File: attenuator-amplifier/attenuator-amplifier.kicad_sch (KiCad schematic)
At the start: 61 parts, among them J1 IN, J2 AOUT, J3 V_{REF}, J4 COM, J5 PWR, K1 G6KU-2, K2 G6KU-2, K3 G6KU-2, U1 DG4052E, U2 OPA197xDBV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

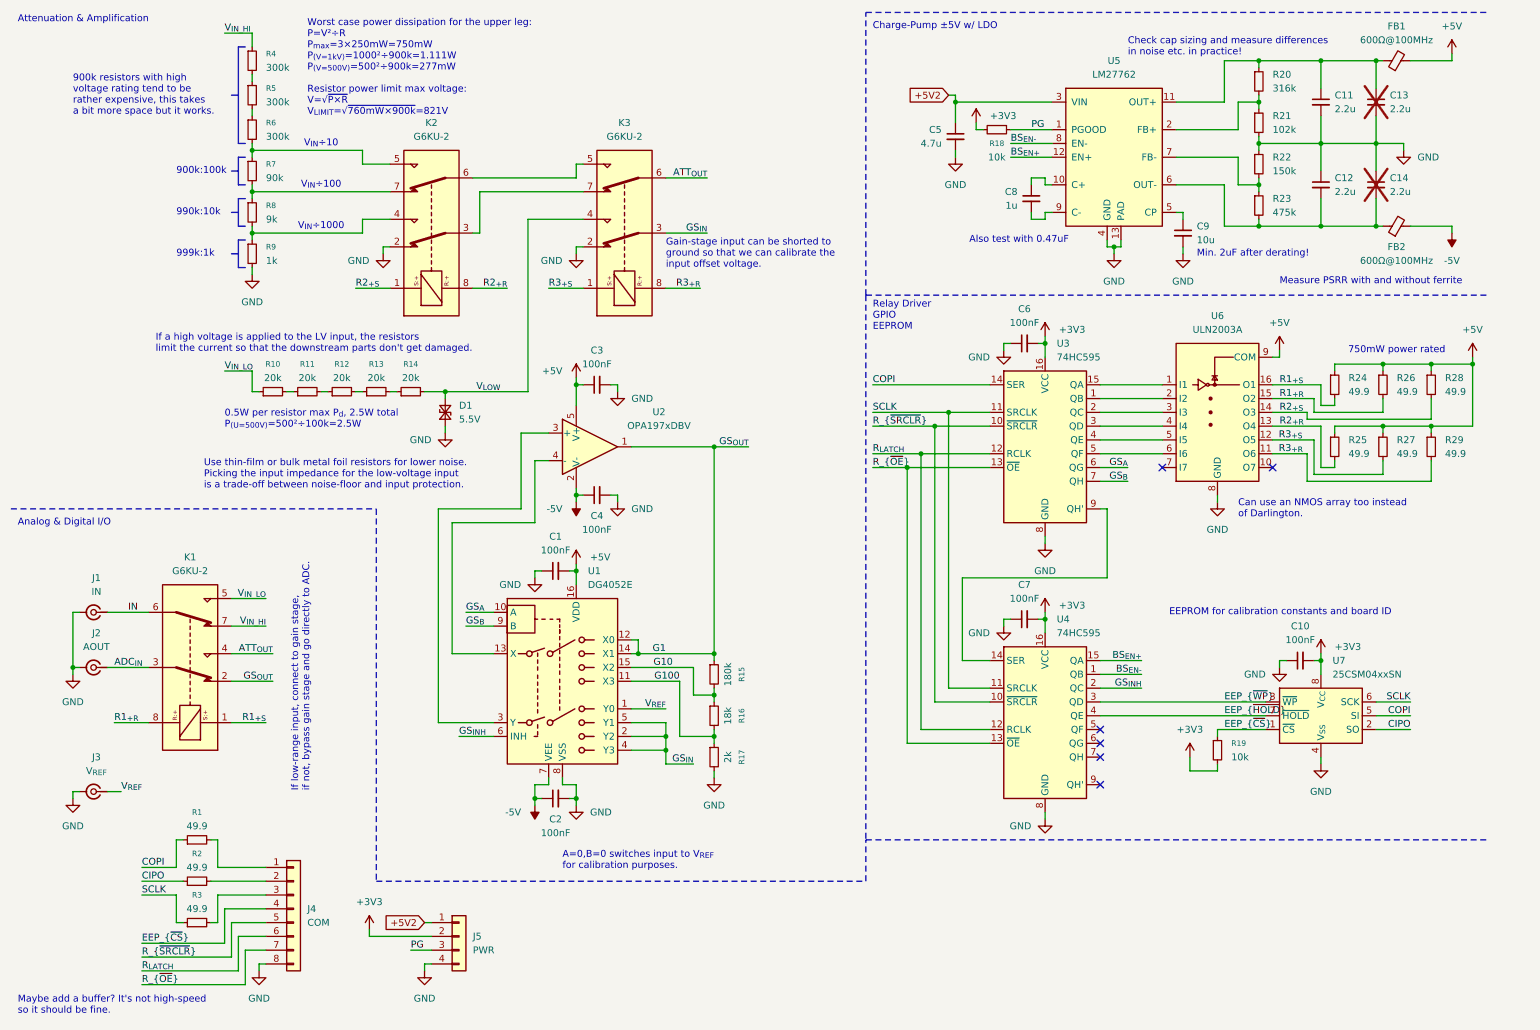
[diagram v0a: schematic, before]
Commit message: small changes, add missing part numbers
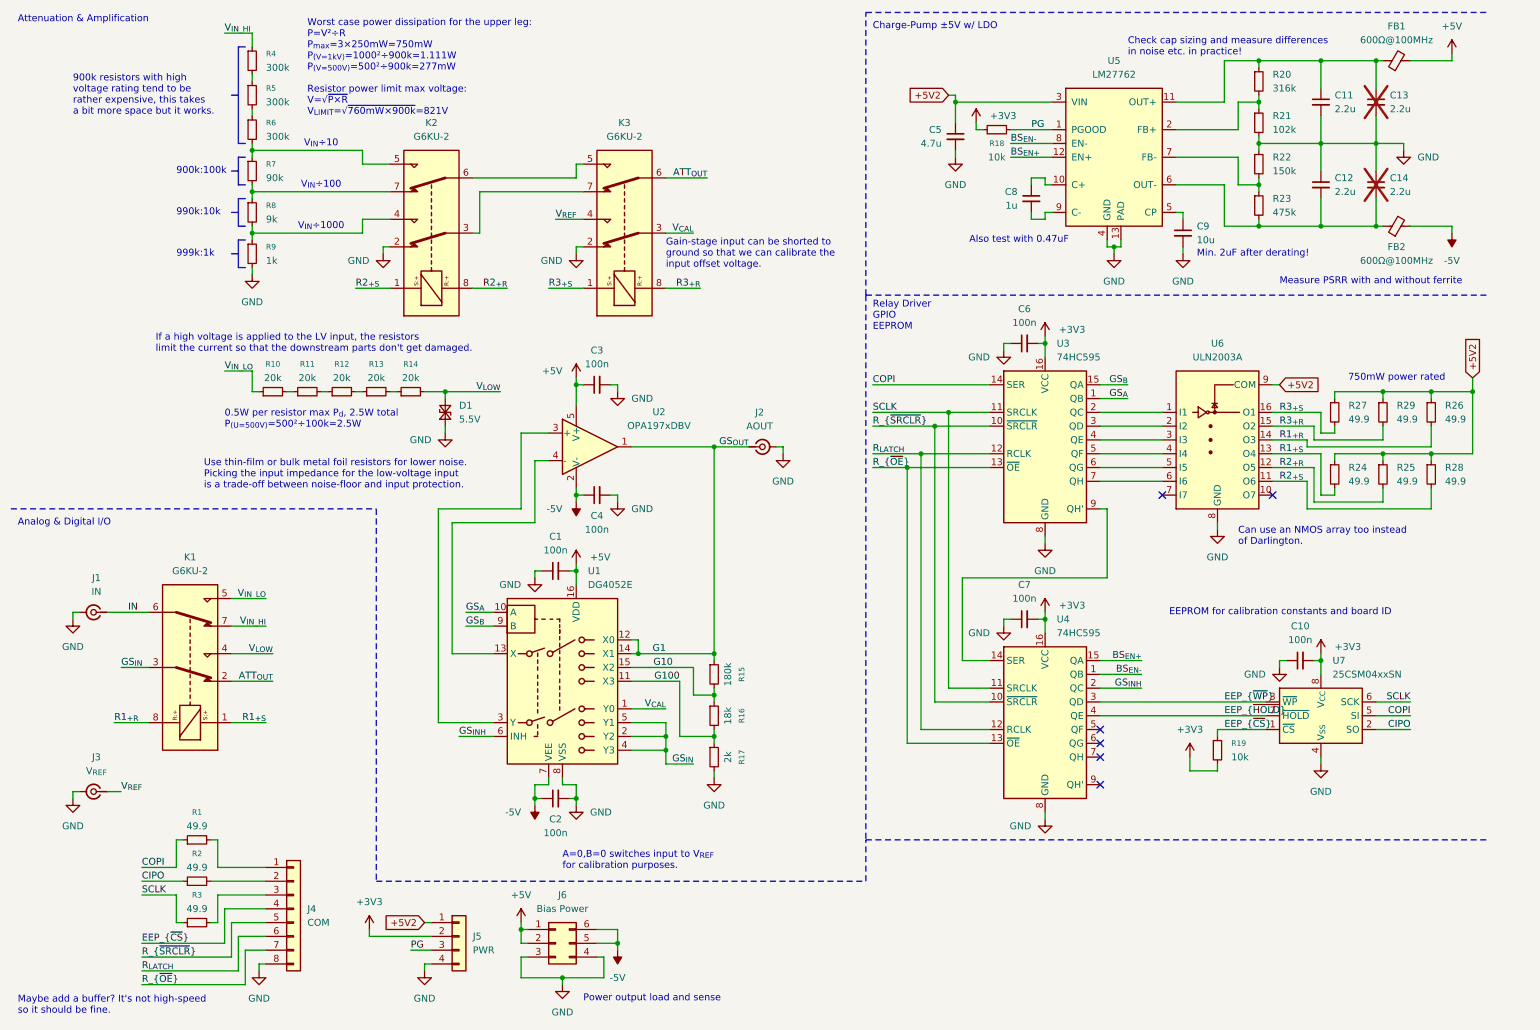
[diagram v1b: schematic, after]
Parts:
- added J6: Bias Power, Connector_PinHeader_2.54mm:PinHeader_2x03_P2.54mm_Vertical, symbol Connector_Generic:Conn_02x03_Counter_Clockwise
- C1, C10, C2, C3, C4, C6, C7: value 100nF -> 100n; MPN (none) -> FN15X104K500PKG
- C11, C12, C13, C14: MPN (none) -> GRM188Z71E225KE43D
- C5: MPN (none) -> TCC0603X7R475K100CT
- C8: MPN (none) -> CGA0603X7R105K250JT
- C9: MPN (none) -> GRM188Z71A106MA73D
- FB1, FB2: MPN (none) -> 74404024220
- J1, J2, J3: MPN (none) -> 61611002121501
- R1, R2, R3: MPN (none) -> 0603WAF499JT5E
- R15: MPN (none) -> RT0603BRB07180KL
- R16: MPN (none) -> RT0603BRB0718KL
- R17: MPN (none) -> AR03BTBX2001
- R18, R19: MPN (none) -> ARG03DTC1002
- R20: MPN (none) -> FRC0402F3163TS
- R21: MPN (none) -> 0402WGF1023TCE
- R22: MPN (none) -> AECR0402F150KK9
- R23: MPN (none) -> HPCR0402F475KK9
- R4, R5, R6: MPN (none) -> RT1206BRD07300KL
- R7: MPN (none) -> RT1206BRE0790KL
- R8: MPN (none) -> RT1206BRD079KL
- R9: MPN (none) -> RT1206BRD071KL
- U1: MPN (none) -> DG4052EEY-T1-GE3
- U2: MPN (none) -> OPA197IDBVT
- U5: MPN (none) -> LM27762DSSR
- U6: MPN (none) -> ULN2003ADR
- U7: MPN (none) -> FT25C32A-USR-T
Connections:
- net +5V: now also J6.1 (Pin_1), J6.2 (Pin_2); no longer R24.1, R25.1, R26.1, R27.1, R28.1, R29.1, U6.9 (COM)
- net +5V2: now also R24.1, R25.1, R26.1, R27.1, R28.1, R29.1, U6.9 (COM)
- net -5V: now also J6.5 (Pin_5), J6.6 (Pin_6)
- net ATT_{OUT}: now also K1.2; no longer K1.4
- net G1: now also J2.1 (In); no longer K1.2
- net GND: now also J6.3 (Pin_3), J6.4 (Pin_4)
- net GS_{A}: now also U3.1 (QB); no longer U3.6 (QG)
- net GS_{B}: now also U3.15 (QA); no longer U3.7 (QH)
- net GS_{IN}: now also K1.3; no longer K3.3
- net R1_{+R}: now also U6.14 (O3); no longer U6.15 (O2)
- net R1_{+S}: now also U6.13 (O4); no longer U6.16 (O1)
- net R2_{+R}: now also U6.12 (O5); no longer U6.13 (O4)
- net R2_{+S}: now also U6.11 (O6); no longer U6.14 (O3)
- net R3_{+R}: now also U6.15 (O2); no longer U6.11 (O6)
- net R3_{+S}: now also U6.16 (O1); no longer U6.12 (O5)
- net V_{LOW}: now also K1.4; no longer K3.4
- net V_{REF}: now also K3.4; no longer U1.1 (Y0)
- net at U6.2 (I2): now also U3.3 (QD); no longer U3.1 (QB)
- net at U6.1 (I1): now also U3.2 (QC); no longer U3.15 (QA)
- net at U6.3 (I3): now also U3.4 (QE); no longer U3.2 (QC)
- net at U6.4 (I4): now also U3.5 (QF); no longer U3.3 (QD)
- net at U6.5 (I5): now also U3.6 (QG); no longer U3.4 (QE)
- net at U6.6 (I6): now also U3.7 (QH); no longer U3.5 (QF)
- removed net ADC_{IN}: J2.1 (In), K1.3
- new net V_{CAL}: K3.3, U1.1 (Y0)
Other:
- note added: "Power output load and sense"
- note removed: "If low-range input, connect to gain stage, if not, bypass gain stage and go directly to ADC."
- moved on the sheet: J2, R24, R25, R26, R27, R28, R29, U6
